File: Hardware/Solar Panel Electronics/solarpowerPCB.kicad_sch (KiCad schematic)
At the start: 17 parts

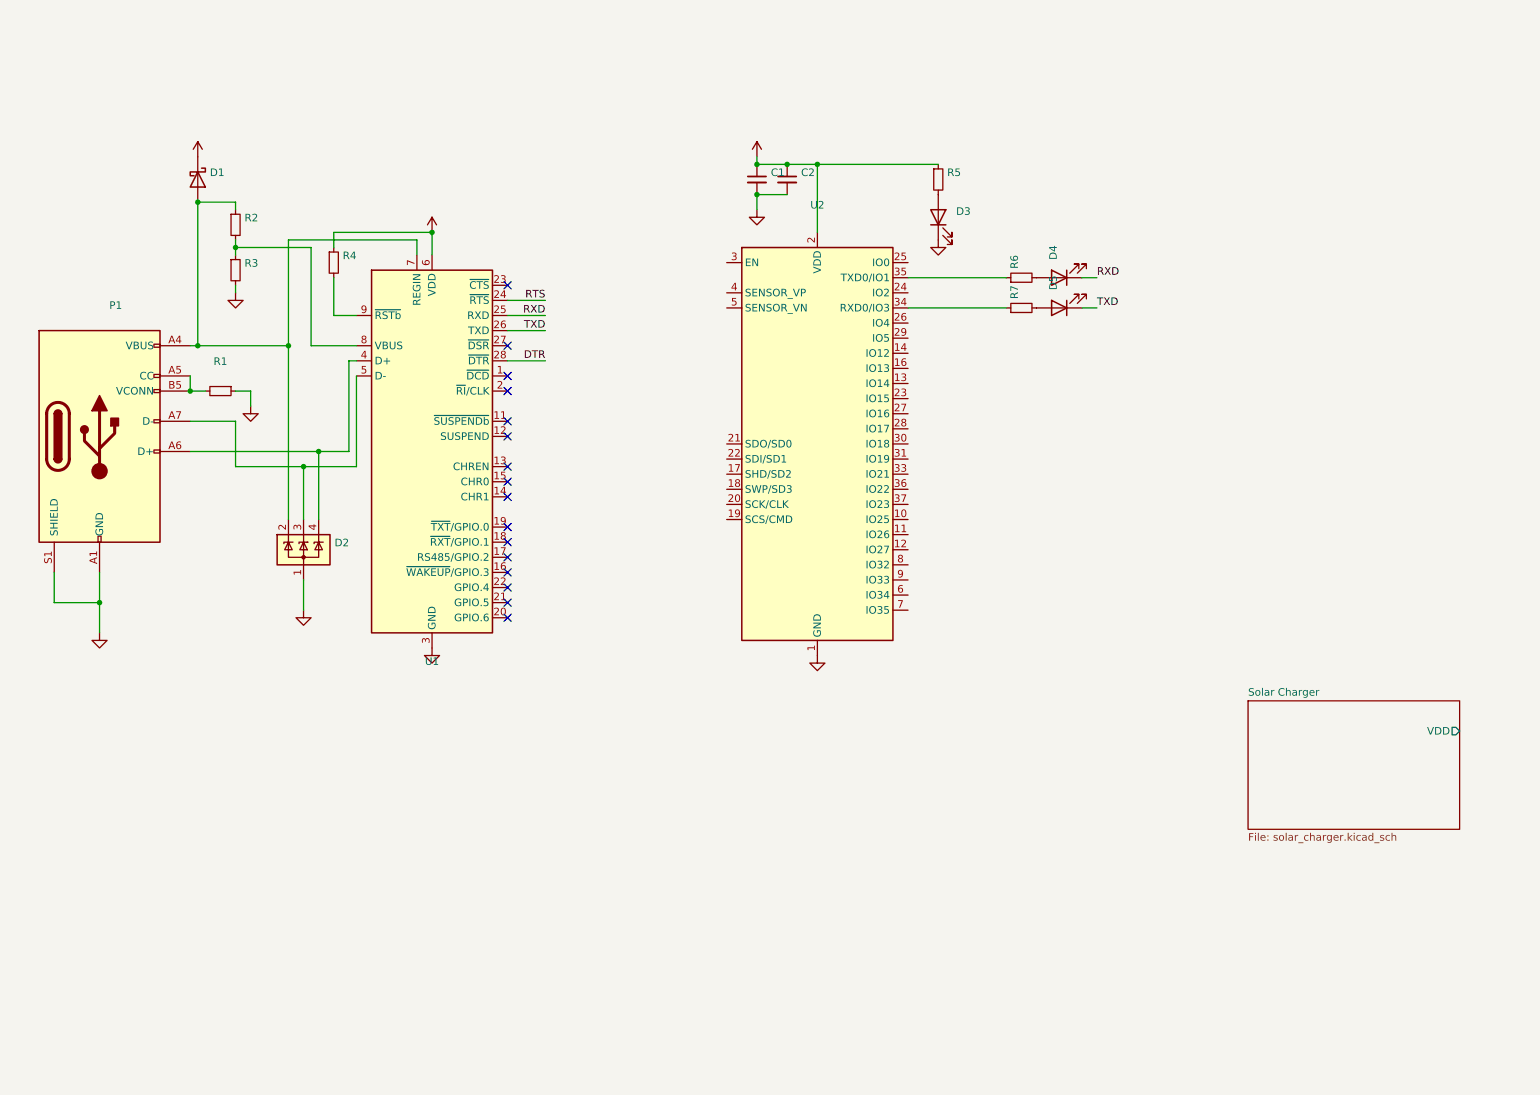
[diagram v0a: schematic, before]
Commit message: Move uart to separate sheet and fix
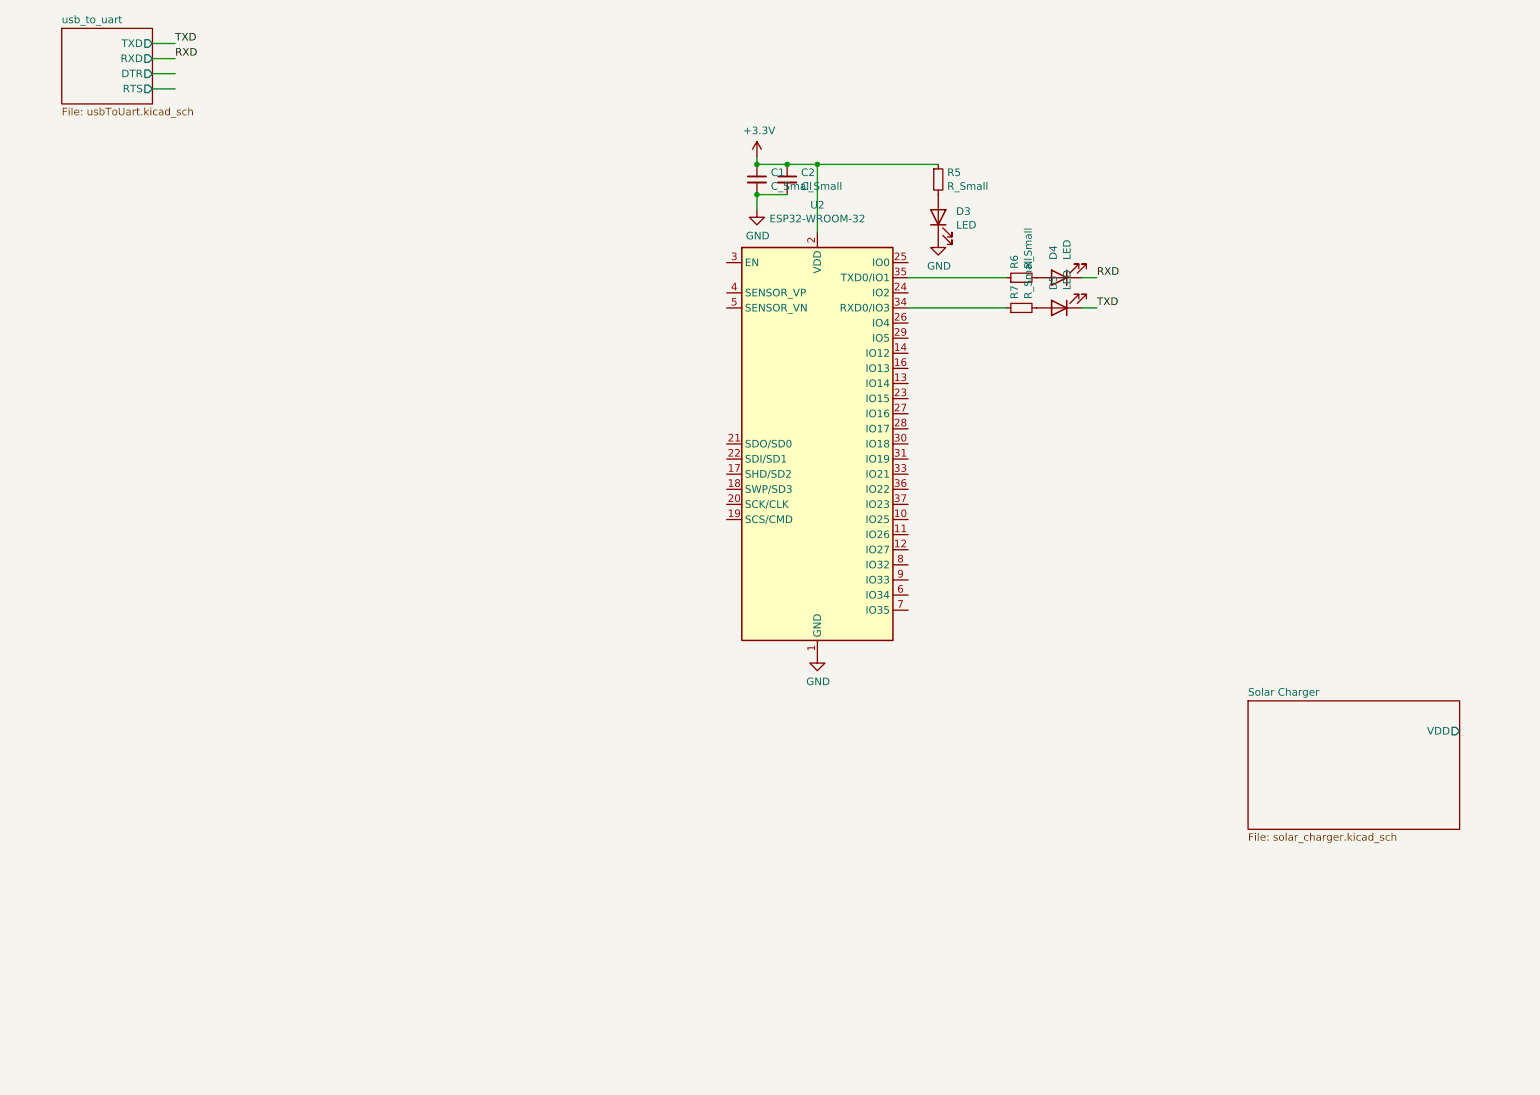
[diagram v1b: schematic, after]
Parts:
- removed D1: (no value), symbol Device:D_Schottky
- removed D2: (no value), symbol Power_Protection:SP0503BAHT
- removed P1: (no value), symbol Connector:USB_C_Plug_USB2.0
- removed R1, R2, R3, R4: (no value), symbol Device:R_Small
- removed U1: (no value), symbol solarpowerPCB-rescue:CP2102N-A01-GQFN28-Interface_USB
- C1, C2: value (none) -> C_Small
- D3, D4, D5: value (none) -> LED
- R5, R6, R7: value (none) -> R_Small
- U2: value (none) -> ESP32-WROOM-32; footprint (none) -> RF_Module:ESP32-WROOM-32
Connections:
- no-connect marks 16 -> 0
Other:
- added sheet usb_to_uart (usbToUart.kicad_sch)

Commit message: Add RICARDO bus and CAN
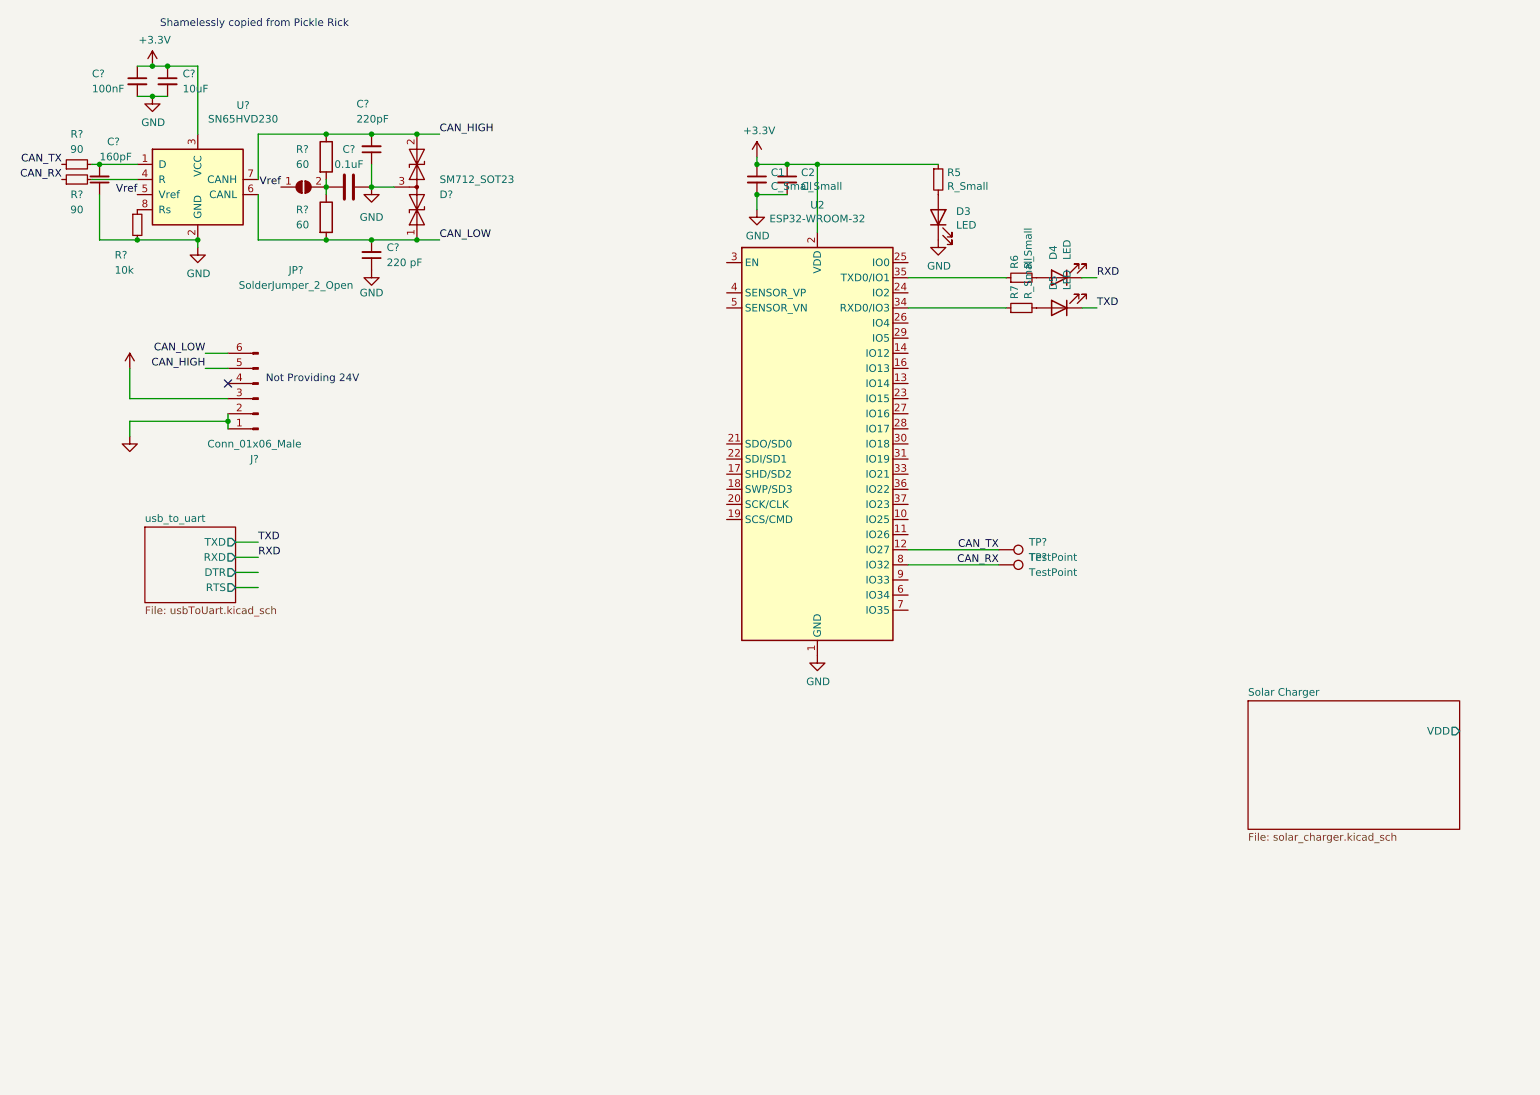
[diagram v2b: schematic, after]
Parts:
- added C?: 100nF, Capacitor_SMD:C_0603_1608Metric, symbol Device:C_Small
- added C?: 220 pF, Capacitor_SMD:C_0603_1608Metric, symbol Device:C_Small
- added C?: 0.1uF, Capacitor_SMD:C_0603_1608Metric, symbol Device:C
- added C?: 10uF, Capacitor_SMD:C_0603_1608Metric, symbol Device:C_Small
- added C?: 160pF, Capacitor_SMD:C_0603_1608Metric, symbol Device:C_Small
- added C?: 220pF, Capacitor_SMD:C_0603_1608Metric, symbol Device:C_Small
- added D?: SM712_SOT23, Package_TO_SOT_SMD:SOT-23, symbol Diode:SM712_SOT23
- added J?: Conn_01x06_Male, Connector_Molex:Molex_Mini-Fit_Jr_5566-06A_2x03_P4.20mm_Vertical, symbol Connector:Conn_01x06_Male
- added JP?: SolderJumper_2_Open, Jumper:SolderJumper-2_P1.3mm_Open_RoundedPad1.0x1.5mm, symbol Jumper:SolderJumper_2_Open
- added R? (x2): 60, Resistor_SMD:R_0603_1608Metric, symbol Device:R
- added R? (x2): 90, Resistor_SMD:R_0603_1608Metric, symbol Device:R_Small
- added R?: 10k, Resistor_SMD:R_0603_1608Metric, symbol Device:R_Small
- added TP? (x2): TestPoint, TestPoint:TestPoint_Pad_D1.0mm, symbol Connector:TestPoint
- added U?: SN65HVD230, Package_SO:SOIC-8_3.9x4.9mm_P1.27mm, symbol Interface_CAN_LIN:SN65HVD230
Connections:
- net +3V3: now also C?.1, C?.1, J?.3 (Pin_3), U?.3 (VCC)
- net GND: now also C?.1, C?.1, C?.1, C?.2, C?.2, C?.2, D?.3 (common), J?.1 (Pin_1), J?.2 (Pin_2), R?.2, U?.2 (GND)
- net CAN_TX: now reaches U2.12 (IO27)
- net CAN_TX: now also R?.1, TP?.1
- net CAN_RX: now reaches U2.8 (IO32)
- net CAN_RX: now also R?.1, TP?.1
- new net: C?.1, JP?.2 (B), R?.1, R?.2
- new net: R?.2, U?.4 (R)
- new net: C?.2, R?.2, U?.1 (D)
- new net: R?.1, U?.8 (Rs)
- new net CAN_HIGH: C?.2, D?.2 (A2), J?.5 (Pin_5), R?.1, U?.7 (CANH)
- new net CAN_LOW: C?.2, D?.1 (A1), J?.6 (Pin_6), R?.2, U?.6 (CANL)
- new net Vref: JP?.1 (A), U?.5 (Vref)
- no-connect marks 0 -> 1
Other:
- note added: "Not Providing 24V"
- note added: "Shamelessly copied from Pickle Rick"

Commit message: Change MCU to PICO-D4
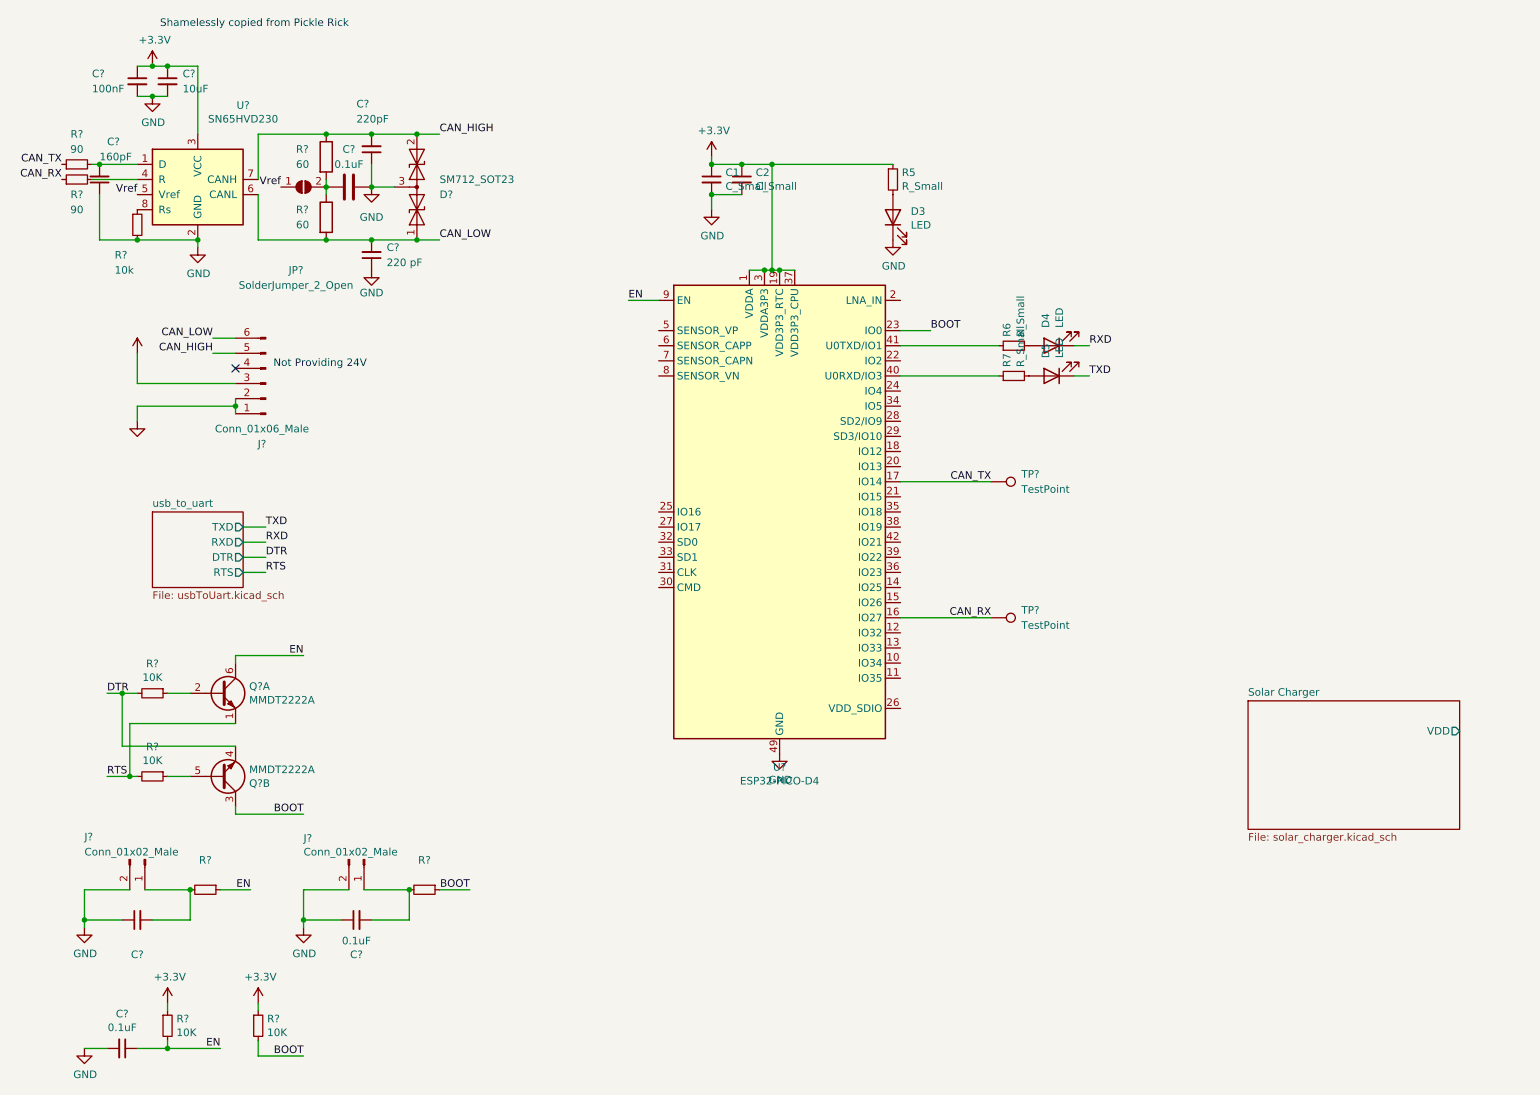
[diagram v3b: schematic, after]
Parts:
- removed U2: ESP32-WROOM-32, RF_Module:ESP32-WROOM-32, symbol RF_Module:ESP32-WROOM-32
- added C? (x2): 0.1uF, Capacitor_SMD:C_0603_1608Metric, symbol Device:C_Small
- added C?: (no value), Capacitor_SMD:C_0603_1608Metric, symbol Device:C_Small
- added J? (x2): Conn_01x02_Male, Connector_PinHeader_2.54mm:PinHeader_1x02_P2.54mm_Vertical, symbol Connector:Conn_01x02_Male
- added Q? (x2): MMDT2222A, Package_TO_SOT_SMD:SOT-363_SC-70-6, symbol Transistor_BJT:MMDT2222A
- added R? (x4): 10K, Resistor_SMD:R_0603_1608Metric, symbol Device:R_Small
- added R? (x2): (no value), Resistor_SMD:R_0603_1608Metric, symbol Device:R_Small
- added U?: ESP32-PICO-D4, Package_DFN_QFN:QFN-48-1EP_7x7mm_P0.5mm_EP5.3x5.3mm, symbol RF_Module:ESP32-PICO-D4
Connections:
- net +3V3: now also R?.1, R?.1, U?.1 (VDDA), U?.19 (VDD3P3_RTC), U?.3 (VDDA3P3), U?.37 (VDD3P3_CPU), U?.4 (VDDA3P3), U?.43 (VDDA), U?.46 (VDDA)
- net CAN_RX: now also U?.16 (IO27)
- net CAN_TX: now also U?.17 (IO14)
- net GND: now also C?.1, C?.1, C?.2, J?.2 (Pin_2), J?.2 (Pin_2), U?.49 (GND)
- net at R7.1: now also U?.40 (U0RXD/IO3)
- net at R6.1: now also U?.41 (U0TXD/IO1)
- new net: C?.2, J?.1 (Pin_1), R?.2 (x2)
- new net: Q?.2 (B1), R?.1
- new net: Q?.5 (B2), R?.1
- new net BOOT: Q?.3 (C2), R?.1, R?.2, U?.23 (IO0)
- new net DTR: Q?.4 (E2), R?.2
- new net EN: C?.1, Q?.6 (C1), R?.1, R?.2, U?.9 (EN)
- new net RTS: Q?.1 (E1), R?.2
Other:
- moved on the sheet: C1, C2, D3, D4, D5, J?, R5, R6, R7, TP?

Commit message: Add SD card
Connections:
- net CAN_RX: now also U?.13 (IO33); no longer U?.16 (IO27)
- net CAN_TX: now also U?.12 (IO32); no longer U?.17 (IO14)
- net SD_CS: now reaches U?.14 (IO25)
- net HSPI_MISO: now reaches U?.18 (IO12)
- net HSPI_MOSI: now reaches U?.20 (IO13)
- new net HSPI_SCLK: U?.17 (IO14)
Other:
- added sheet Storage (storage_sch.kicad_sch)
- moved on the sheet: TP?

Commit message: Edited the charging circuit, need to resize components
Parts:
- C?: value (none) -> 1uF
- R? (x2): value (none) -> 0
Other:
- sheet Solar Charger ports: added Vout; removed VDD
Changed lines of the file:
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@@
     (in_bom yes) (on_board yes)
     (property "Reference" "R?" (id 0) (at 44.45 156.3116 90))
-    (property "Value" "" (id 1) (at 44.45 158.623 90))
+    (property "Value" "0" (id 1) (at 44.45 158.623 90))
     (property "Footprint" "Resistor_SMD:R_0603_1608Metric" (id 2) (at 44.45 161.29 0)
       (effects (font (size 1.27 1.27)) hide)
@@
     (in_bom yes) (on_board yes)
     (property "Reference" "R?" (id 0) (at 81.28 156.3116 90))
-    (property "Value" "" (id 1) (at 81.28 158.623 90))
+    (property "Value" "0" (id 1) (at 81.28 158.623 90))
     (property "Footprint" "Resistor_SMD:R_0603_1608Metric" (id 2) (at 81.28 161.29 0)
       (effects (font (size 1.27 1.27)) hide)
@@
       (effects (font (size 1.27 1.27)) hide)
     )
-    (property "Value" "" (id 1) (at 33.02 66.04 0))
+    (property "Value" "+3.3V" (id 1) (at 33.02 66.04 0))
     (property "Footprint" "" (id 2) (at 33.02 71.12 0)
       (effects (font (size 1.27 1.27)) hide)
@@
     (in_bom yes) (on_board yes)
     (property "Reference" "C?" (id 0) (at 33.02 172.1866 90))
-    (property "Value" "" (id 1) (at 33.02 169.8752 90))
+    (property "Value" "1uF" (id 1) (at 33.02 169.8752 90))
     (property "Footprint" "Capacitor_SMD:C_0603_1608Metric" (id 2) (at 33.02 166.37 0)
       (effects (font (size 1.27 1.27)) hide)
@@
       (effects (font (size 1.27 1.27)) hide)
     )
-    (property "Value" "" (id 1) (at 33.02 87.63 0))
+    (property "Value" "GND" (id 1) (at 33.02 87.63 0))
     (property "Footprint" "" (id 2) (at 33.02 82.55 0)
       (effects (font (size 1.27 1.27)) hide)
@@
       (effects (font (size 1.27 1.27)) (justify left top))
     )
-    (pin "VDD" output (at 255.27 134.62 0)
+    (pin "Vout" output (at 255.27 134.62 0)
       (effects (font (size 1.27 1.27)) (justify right))
     )
@@
   )
   (symbol_instances
-    (path "/00000000-0000-0000-0000-0000624b2440/00000000-0000-0000-0000-00006248d5be"
-      (reference "#PWR0101") (unit 1) (value "GND") (footprint "")
-    )
     (path "/00000000-0000-0000-0000-0000624b2440/00000000-0000-0000-0000-00006248f76c"
       (reference "#PWR0102") (unit 1) (value "GND") (footprint "")
@@
       (reference "D?") (unit 1) (value "USB_LED") (footprint "LED_SMD:LED_0603_1608Metric")
     )
+    (path "/00000000-0000-0000-0000-0000624b2440/73f4fb04-7f3b-4979-a37a-df6982c73ad3"
+      (reference "D?") (unit 1) (value "D_Schottky") (footprint "")
+    )
     (path "/761ca562-7e61-4873-a476-3f17aaa1ae77/9d8eb635-b541-4cc6-a0c2-2d8a2a232914"
